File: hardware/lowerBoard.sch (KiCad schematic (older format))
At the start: 8 parts, among them J3 Conn_02x10_Odd_Even, J4 Screw_Terminal_01x09, J5 Screw_Terminal_01x09, J6 Screw_Terminal_01x08, J7 Screw_Terminal_01x08, U5 R-783.3-0.5

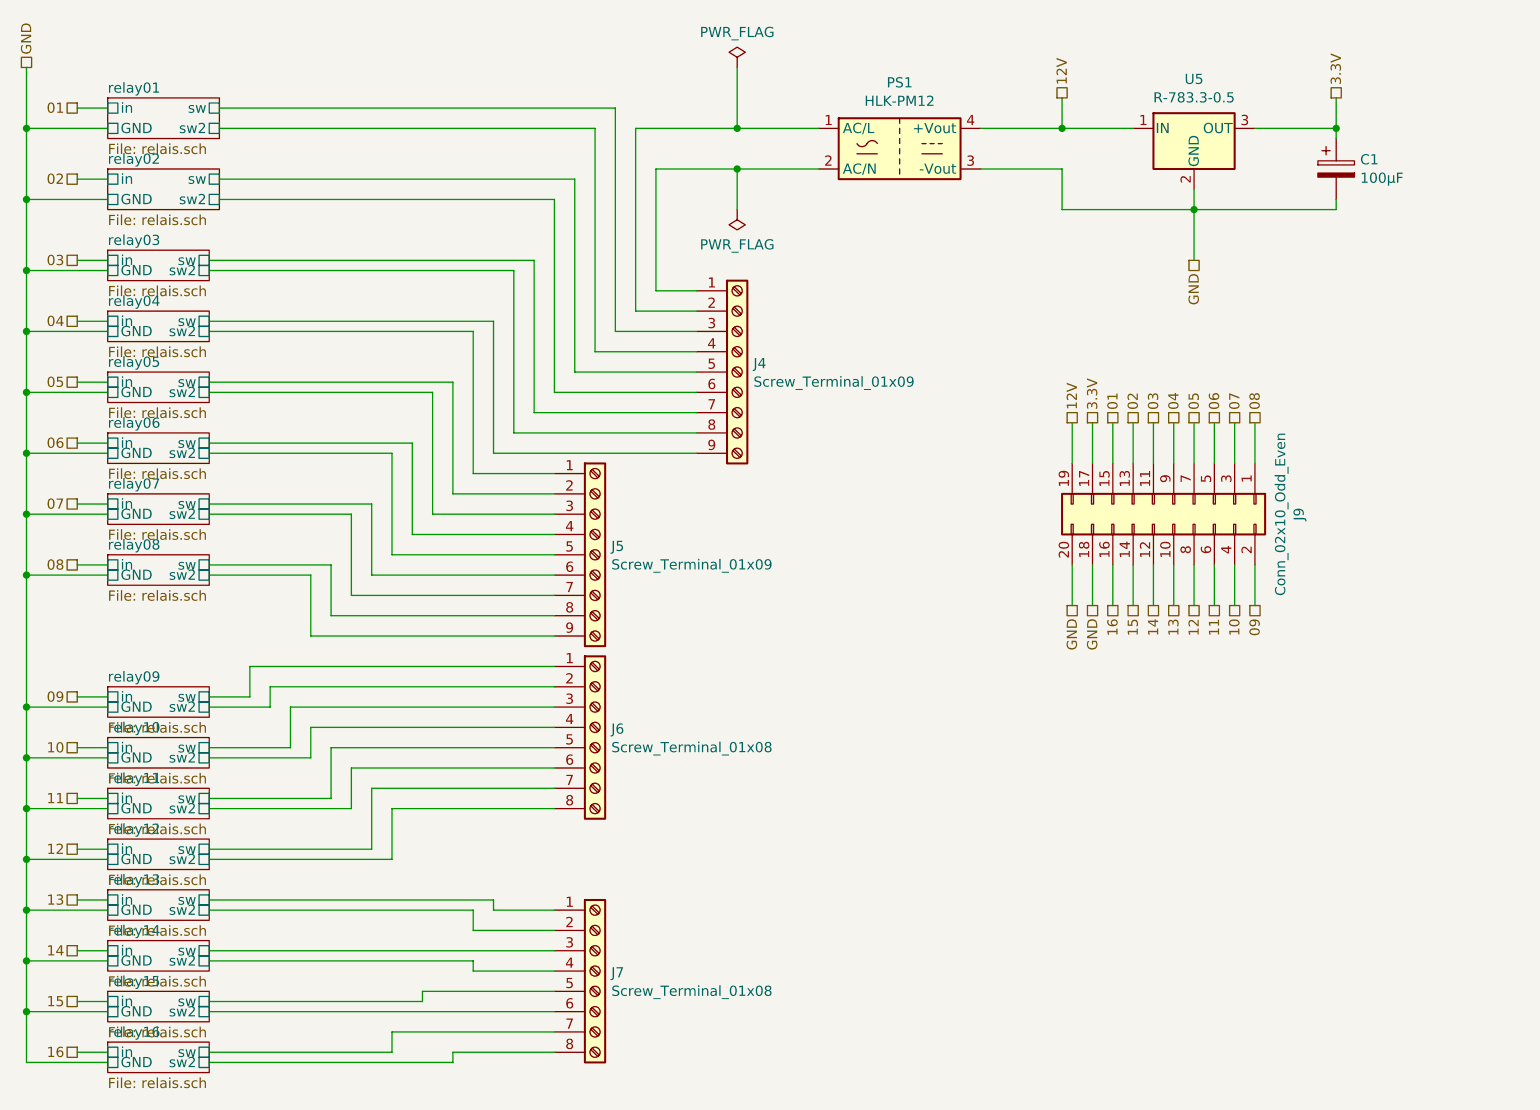
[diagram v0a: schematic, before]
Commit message: move on to 16A relays
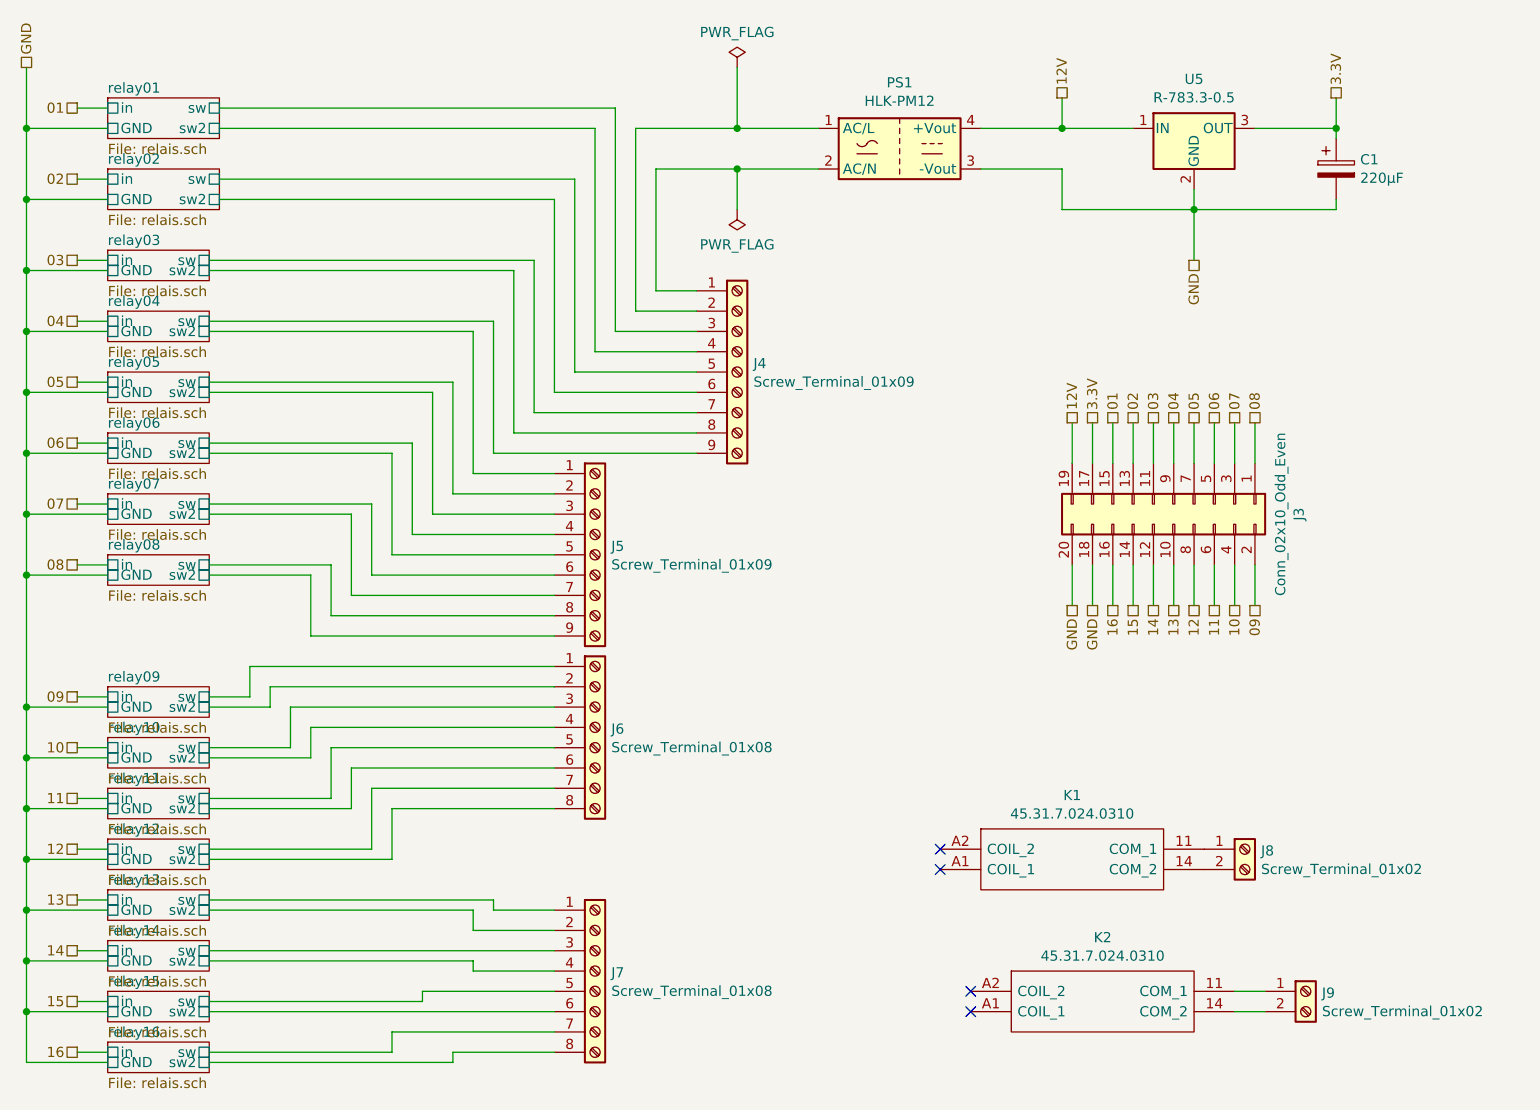
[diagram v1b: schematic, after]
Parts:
- added J8, J9: Screw_Terminal_01x02, TerminalBlock_MetzConnect:TerminalBlock_MetzConnect_Type101_RT01602HBWC_1x02_P5.08mm_Horizontal, symbol Connector:Screw_Terminal_01x02
- added K1, K2: 45.31.7.024.0310, Finder:finder-45.31.7.024.0310, symbol Finder_45.31:45.31.7.024.0310
- C1: value 100µF -> 220µF
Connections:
- new net: J8.1 (Pin_1), K1.11 (COM_1)
- new net: J8.2 (Pin_2), K1.14 (COM_2)
- new net: J9.1 (Pin_1), K2.11 (COM_1)
- new net: J9.2 (Pin_2), K2.14 (COM_2)
- no-connect marks 0 -> 4
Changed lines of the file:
@@
 $Descr A4 11693 8268
 encoding utf-8
-Sheet 1 17
+Sheet 3 19
 Title ""
 Date ""
@@
 P 8100 1200
 F 0 "C1" H 8218 1246 50  0000 L CNN
-F 1 "100µF" H 8218 1155 50  0000 L CNN
+F 1 "220µF" H 8218 1155 50  0000 L CNN
 F 2 "Capacitor_THT:CP_Radial_D6.3mm_P2.50mm" H 8138 1050 50  0001 C CNN
 F 3 "~" H 8100 1200 50  0001 C CNN
@@
 AR Path="/5D9B8E7D/5DC1CA09" Ref="J?"  Part="1"
 AR Path="/5D9FF064/5DC1CA09" Ref="J3"  Part="1"
-AR Path="/5DC1CA09" Ref="J9"  Part="1"
-F 0 "J9" H 7350 3467 50  0000 C CNN
+AR Path="/5DC1CA09" Ref="J3"  Part="1"
+F 0 "J3" H 7350 3467 50  0000 C CNN
 F 1 "Conn_02x10_Odd_Even" H 7350 3376 50  0000 C CNN
 F 2 "Connector_PinHeader_2.54mm:PinHeader_2x10_P2.54mm_Vertical" H 7300 2850 50  0001 C CNN
@@
 Wire Wire Line
 	5150 1000 5550 1000
+$Comp
+L Connector:Screw_Terminal_01x02 J8
+U 1 1 6014E5F9
+P 7650 4550
+F 0 "J8" H 7730 4542 50  0000 L CNN
+F 1 "Screw_Terminal_01x02" H 7730 4451 50  0000 L CNN
+F 2 "TerminalBlock_MetzConnect:TerminalBlock_MetzConnect_Type101_RT01602HBWC_1x02_P5.08mm_Horizontal" H 7650 4550 50  0001 C CNN
+F 3 "~" H 7650 4550 50  0001 C CNN
+	1    7650 4550
+	1    0    0    -1
+$EndComp
+NoConn ~ 6150 4550
+NoConn ~ 6150 4650
+$Comp
+L Connector:Screw_Terminal_01x02 J9
+U 1 1 601E84EE
+P 7950 5250
+F 0 "J9" H 8030 5242 50  0000 L CNN
+F 1 "Screw_Terminal_01x02" H 8030 5151 50  0000 L CNN
+F 2 "TerminalBlock_MetzConnect:TerminalBlock_MetzConnect_Type101_RT01602HBWC_1x02_P5.08mm_Horizontal" H 7950 5250 50  0001 C CNN
+F 3 "~" H 7950 5250 50  0001 C CNN
+	1    7950 5250
+	1    0    0    -1
+$EndComp
+$Comp
+L Finder_45.31:45.31.7.024.0310 K2
+U 1 1 601E88F3
+P 6300 5250
+F 0 "K2" H 6950 5515 50  0000 C CNN
+F 1 "45.31.7.024.0310" H 6950 5424 50  0000 C CNN
+F 2 "Finder:finder-45.31.7.024.0310" H 7450 5350 50  0001 L CNN
+F 3 "http://uk.rs-online.com/web/p/products/7495130" H 7450 5250 50  0001 L CNN
+F 4 "SP-NO PCB Mount Non-Latching Relay Tab, 24V dc" H 7450 5150 50  0001 L CNN "Description"
+F 5 "28.5" H 7450 5050 50  0001 L CNN "Height"
+F 6 "FINDER" H 7450 4950 50  0001 L CNN "Manufacturer_Name"
+F 7 "45.31.7.024.0310" H 7450 4850 50  0001 L CNN "Manufacturer_Part_Number"
+F 8 "" H 7450 4750 50  0001 L CNN "Mouser Part Number"
+F 9 "" H 7450 4650 50  0001 L CNN "Mouser Price/Stock"
+F 10 "" H 7450 4550 50  0001 L CNN "Arrow Part Number"
+F 11 "" H 7450 4450 50  0001 L CNN "Arrow Price/Stock"
+	1    6300 5250
+	1    0    0    -1
+$EndComp
+Wire Wire Line
+	7750 5350 7600 5350
+Wire Wire Line
+	7600 5250 7750 5250
+NoConn ~ 6300 5250
+NoConn ~ 6300 5350
+$Comp
+L Finder_45.31:45.31.7.024.0310 K1
+U 1 1 601A2ACE
+P 6150 4550
+F 0 "K1" H 6800 4815 50  0000 C CNN
+F 1 "45.31.7.024.0310" H 6800 4724 50  0000 C CNN
+F 2 "Finder:finder-45.31.7.024.0310" H 7300 4650 50  0001 L CNN
+F 3 "http://uk.rs-online.com/web/p/products/7495130" H 7300 4550 50  0001 L CNN
+F 4 "SP-NO PCB Mount Non-Latching Relay Tab, 24V dc" H 7300 4450 50  0001 L CNN "Description"
+F 5 "28.5" H 7300 4350 50  0001 L CNN "Height"
+F 6 "FINDER" H 7300 4250 50  0001 L CNN "Manufacturer_Name"
+F 7 "45.31.7.024.0310" H 7300 4150 50  0001 L CNN "Manufacturer_Part_Number"
+F 8 "" H 7300 4050 50  0001 L CNN "Mouser Part Number"
+F 9 "" H 7300 3950 50  0001 L CNN "Mouser Price/Stock"
+F 10 "" H 7300 3850 50  0001 L CNN "Arrow Part Number"
+F 11 "" H 7300 3750 50  0001 L CNN "Arrow Price/Stock"
+	1    6150 4550
+	1    0    0    -1
+$EndComp
 $EndSCHEMATC
